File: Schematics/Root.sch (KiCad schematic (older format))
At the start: 2 parts

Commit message: Updated schematics
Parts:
- removed ANT1: ANT, Pin_Headers:Pin_Header_Straight_1x02, symbol INDUCTOR
- removed C1: C, symbol C
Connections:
- net labels added: SCL, SDA, VPP, Vusb, ~OE[0..12]
- net labels removed: GND
- wire segments 9 -> 7
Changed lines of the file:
@@
 LIBS:pca9685
 LIBS:avr_jtag_header
+LIBS:linear-technology
 LIBS:Root-cache
 EELAYER 25 0
@@
 $Descr A4 11693 8268
 encoding utf-8
-Sheet 1 17
+Sheet 1 16
 Title "RGB Clock"
 Date "Wed 07 Jan 2015"
@@
 $EndDescr
 $Sheet
-S 3850 2200 800  450
-U 54AA18DD
-F0 "Amp and Filter" 60
-F1 "BPF.sch" 60
-F2 "RF_in" I L 3850 2450 60
-F3 "RF_out" I R 4650 2450 60
-$EndSheet
-$Comp
-L INDUCTOR ANT1
-U 1 1 54AA1EFE
-P 3100 2800
-F 0 "ANT1" V 3050 2800 40  0000 C CNN
-F 1 "ANT" V 3200 2800 40  0000 C CNN
-F 2 "Pin_Headers:Pin_Header_Straight_1x02" H 3100 2800 60  0001 C CNN
-F 3 "" H 3100 2800 60  0000 C CNN
-	1    3100 2800
-	1    0    0    -1
-$EndComp
-$Comp
-L C C1
-U 1 1 54AA1FB2
-P 3400 2800
-F 0 "C1" H 3400 2900 40  0000 L CNN
-F 1 "C" H 3406 2715 40  0000 L CNN
-F 2 "" H 3438 2650 30  0001 C CNN
-F 3 "" H 3400 2800 60  0000 C CNN
-	1    3400 2800
-	1    0    0    -1
-$EndComp
-$Comp
-L GND #PWR01
-U 1 1 54AA202B
-P 3250 3200
-F 0 "#PWR01" H 3250 2950 60  0001 C CNN
-F 1 "GND" H 3250 3050 60  0000 C CNN
-F 2 "" H 3250 3200 60  0000 C CNN
-F 3 "" H 3250 3200 60  0000 C CNN
-	1    3250 3200
-	1    0    0    -1
-$EndComp
-Wire Wire Line
-	3250 3200 3250 3100
-Wire Wire Line
-	3100 3100 3400 3100
-Wire Wire Line
-	3400 3100 3400 3000
-Connection ~ 3250 3100
-Wire Wire Line
-	3100 2500 3100 2450
-Wire Wire Line
-	3100 2450 3850 2450
-Wire Wire Line
-	3400 2600 3400 2450
-Connection ~ 3400 2450
-$Sheet
 S 5300 2250 1150 600
 U 54B117F3
@@
 F2 "SDA" B R 6450 2600 60
 F3 "SCL" O R 6450 2750 60
-F4 "RF_In" I L 5300 2450 60
-F5 "~OE[1..12]" O R 6450 2450 60
+F4 "~OE[1..12]" O R 6450 2450 60
+F5 "Vusb" O L 5300 2700 60
+F6 "SNS[0..6]" I L 5300 2350 60
+F7 "SNSK[0..6]" I L 5300 2500 60
 $EndSheet
 $Sheet
@@
 $EndSheet
 $Sheet
-S 1900 4250 1500 1500
+S 5300 3400 1100 450
 U 54B1185F
 F0 "Power Supply" 60
 F1 "PowerSupply.sch" 60
+F2 "Vin" I L 5300 3600 60
+F3 "Vsupply" O R 6400 3600 60
 $EndSheet
 Wire Bus Line
@@
 Wire Wire Line
 	6450 2600 8000 2600
+$Comp
+L VPP #PWR02
+U 1 1 54BAF809
+P 6550 3550
+F 0 "#PWR02" H 6550 3400 60  0001 C CNN
+F 1 "VPP" H 6550 3700 60  0000 C CNN
+F 2 "" H 6550 3550 60  0000 C CNN
+F 3 "" H 6550 3550 60  0000 C CNN
+	1    6550 3550
+	1    0    0    -1
+$EndComp
 Wire Wire Line
-	4650 2450 5300 2450
+	5300 3600 5150 3600
+Wire Wire Line
+	5150 3600 5150 2700
+Wire Wire Line
+	5150 2700 5300 2700
+Wire Wire Line
+	6400 3600 6550 3600
+Wire Wire Line
+	6550 3600 6550 3550
+Text Label 7050 2450 0    60   ~ 0
+~OE[0..12]
+Text Label 7050 2600 0    60   ~ 0
+SDA
+Text Label 7050 2750 0    60   ~ 0
+SCL
+Text Label 5150 3200 0    60   ~ 0
+Vusb
 $EndSCHEMATC

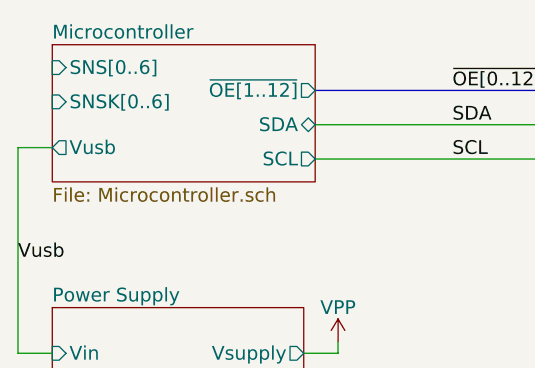
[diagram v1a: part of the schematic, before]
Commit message: Removed RF. Placed all LED drivers and passives and begun routing
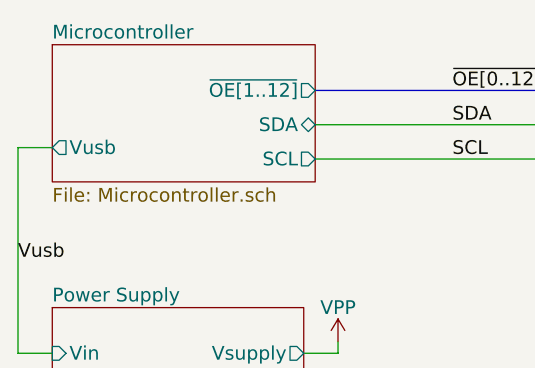
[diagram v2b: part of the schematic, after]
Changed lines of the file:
@@
 F4 "~OE[1..12]" O R 6450 2450 60
 F5 "Vusb" O L 5300 2700 60
-F6 "SNS[0..6]" I L 5300 2350 60
-F7 "SNSK[0..6]" I L 5300 2500 60
 $EndSheet
 $Sheet
@@
 	6450 2600 8000 2600
 $Comp
-L VPP #PWR02
+L VPP #PWR01
 U 1 1 54BAF809
 P 6550 3550
-F 0 "#PWR02" H 6550 3400 60  0001 C CNN
+F 0 "#PWR01" H 6550 3400 60  0001 C CNN
 F 1 "VPP" H 6550 3700 60  0000 C CNN
 F 2 "" H 6550 3550 60  0000 C CNN

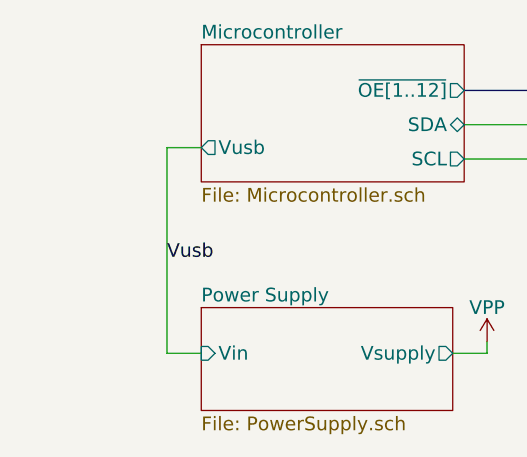
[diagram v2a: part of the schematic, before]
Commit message: Added power in connector in schematics. #3
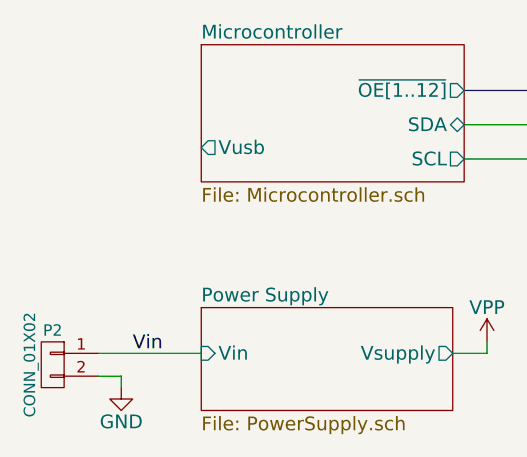
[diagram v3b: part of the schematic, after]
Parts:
- added P2: CONN_01X02, symbol CONN_01X02
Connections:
- new net GND: P2.2 (P2)
- new net Vin: P2.1 (P1)
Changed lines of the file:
@@
 	6450 2600 8000 2600
 $Comp
-L VPP #PWR01
+L VPP #PWR2
 U 1 1 54BAF809
 P 6550 3550
-F 0 "#PWR01" H 6550 3400 60  0001 C CNN
+F 0 "#PWR2" H 6550 3400 60  0001 C CNN
 F 1 "VPP" H 6550 3700 60  0000 C CNN
 F 2 "" H 6550 3550 60  0000 C CNN
@@
 $EndComp
 Wire Wire Line
-	5300 3600 5150 3600
-Wire Wire Line
-	5150 3600 5150 2700
-Wire Wire Line
-	5150 2700 5300 2700
+	4850 3600 5300 3600
 Wire Wire Line
 	6400 3600 6550 3600
@@
 Text Label 7050 2750 0    60   ~ 0
 SCL
-Text Label 5150 3200 0    60   ~ 0
-Vusb
+$Comp
+L CONN_01X02 P2
+U 1 1 54C94425
+P 4650 3650
+F 0 "P2" H 4650 3800 50  0000 C CNN
+F 1 "CONN_01X02" V 4750 3650 50  0000 C CNN
+F 2 "" H 4650 3650 60  0000 C CNN
+F 3 "" H 4650 3650 60  0000 C CNN
+	1    4650 3650
+	-1   0    0    -1
+$EndComp
+$Comp
+L GND #PWR1
+U 1 1 54C94A98
+P 4950 3750
+F 0 "#PWR1" H 4950 3500 60  0001 C CNN
+F 1 "GND" H 4950 3600 60  0000 C CNN
+F 2 "" H 4950 3750 60  0000 C CNN
+F 3 "" H 4950 3750 60  0000 C CNN
+	1    4950 3750
+	1    0    0    -1
+$EndComp
+Wire Wire Line
+	4850 3700 4950 3700
+Wire Wire Line
+	4950 3700 4950 3750
+Text Label 5000 3600 0    60   ~ 0
+Vin
 $EndSCHEMATC

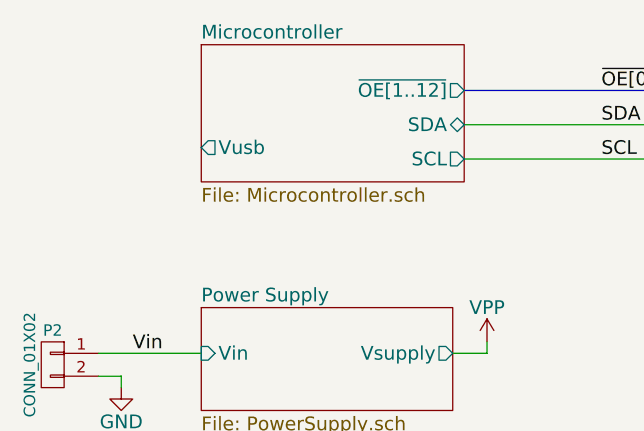
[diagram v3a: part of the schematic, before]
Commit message: Added some switches for interface #7
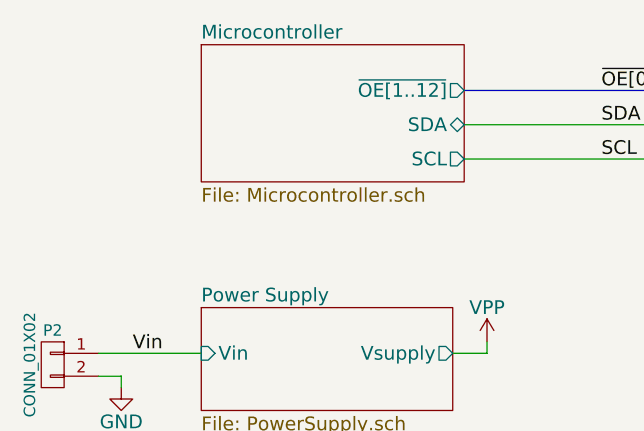
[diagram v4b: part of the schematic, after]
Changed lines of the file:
@@
 F3 "SCL" O R 6450 2750 60
 F4 "~OE[1..12]" O R 6450 2450 60
-F5 "Vusb" O L 5300 2700 60
 $EndSheet
 $Sheet

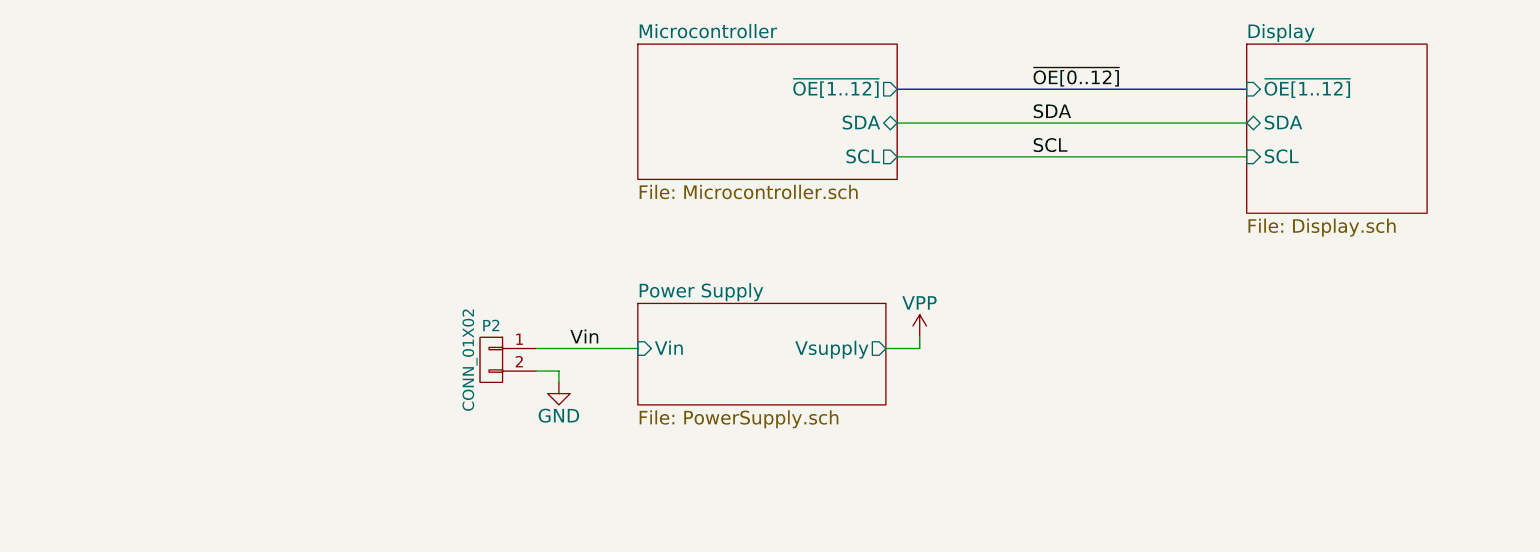
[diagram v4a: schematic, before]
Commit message: Changed lots
Finalised the Inductor. Closes #5
Changed USB Connector. Closes #4
Added four switches for a simple interface. Closes #7
Added a power jack. Closes #3
Found RTC Oscillator. Closes #1.
Added part numbers to all major components. Closes #2
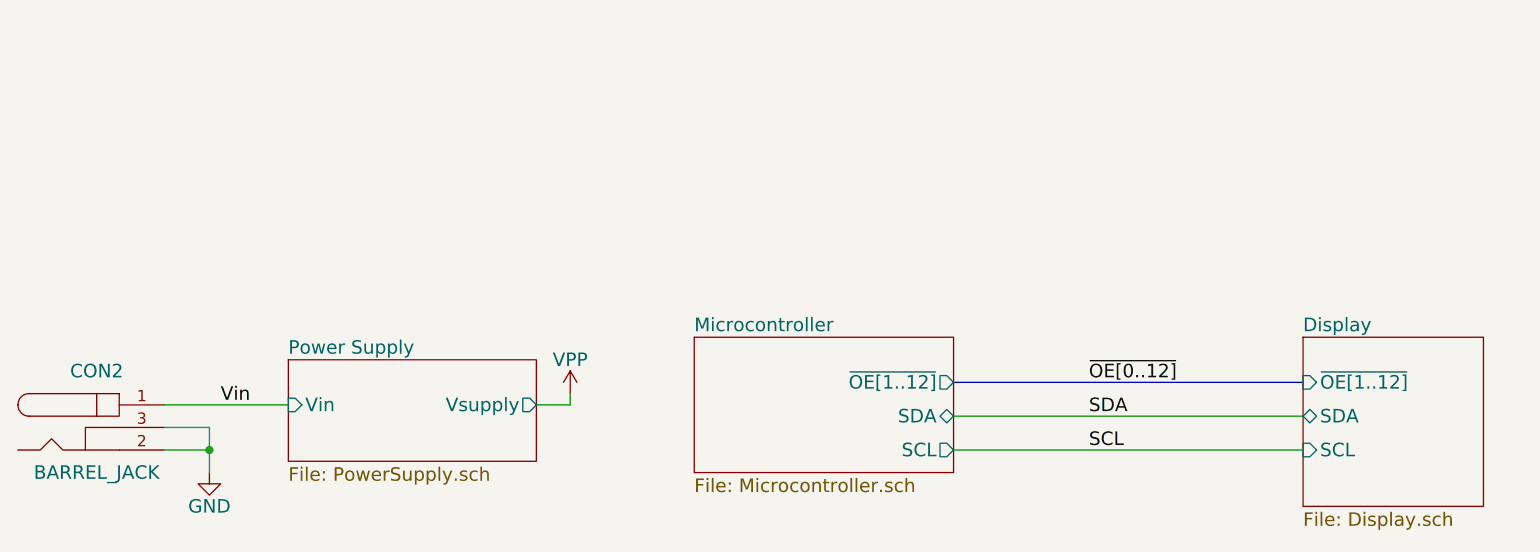
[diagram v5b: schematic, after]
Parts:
- removed P2: CONN_01X02, symbol CONN_01X02
- added CON2: BARREL_JACK, Connect:JACK_ALIM, symbol BARREL_JACK
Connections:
- net GND: now also CON2.2, CON2.3
- net Vin: now also CON2.1
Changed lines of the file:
@@
 $EndDescr
 $Sheet
-S 5300 2250 1150 600
+S 5550 3550 1150 600
 U 54B117F3
 F0 "Microcontroller" 60
 F1 "Microcontroller.sch" 60
-F2 "SDA" B R 6450 2600 60
-F3 "SCL" O R 6450 2750 60
-F4 "~OE[1..12]" O R 6450 2450 60
+F2 "SDA" B R 6700 3900 60
+F3 "SCL" O R 6700 4050 60
+F4 "~OE[1..12]" O R 6700 3750 60
 $EndSheet
 $Sheet
-S 8000 2250 800  750
+S 8250 3550 800  750
 U 54B11834
 F0 "Display" 60
 F1 "Display.sch" 60
-F2 "SDA" B L 8000 2600 60
-F3 "SCL" I L 8000 2750 60
-F4 "~OE[1..12]" I L 8000 2450 60
+F2 "SDA" B L 8250 3900 60
+F3 "SCL" I L 8250 4050 60
+F4 "~OE[1..12]" I L 8250 3750 60
 $EndSheet
 $Sheet
-S 5300 3400 1100 450
+S 3750 3650 1100 450
 U 54B1185F
 F0 "Power Supply" 60
 F1 "PowerSupply.sch" 60
-F2 "Vin" I L 5300 3600 60
-F3 "Vsupply" O R 6400 3600 60
+F2 "Vin" I L 3750 3850 60
+F3 "Vsupply" O R 4850 3850 60
 $EndSheet
 Wire Bus Line
-	6450 2450 8000 2450
+	6700 3750 8250 3750
 Wire Wire Line
-	8000 2750 6450 2750
+	8250 4050 6700 4050
 Wire Wire Line
-	6450 2600 8000 2600
+	6700 3900 8250 3900
 $Comp
-L VPP #PWR2
+L VPP #PWR01
 U 1 1 54BAF809
-P 6550 3550
-F 0 "#PWR2" H 6550 3400 60  0001 C CNN
-F 1 "VPP" H 6550 3700 60  0000 C CNN
-F 2 "" H 6550 3550 60  0000 C CNN
-F 3 "" H 6550 3550 60  0000 C CNN
-	1    6550 3550
+P 5000 3800
+F 0 "#PWR01" H 5000 3650 60  0001 C CNN
+F 1 "VPP" H 5000 3950 60  0000 C CNN
+F 2 "" H 5000 3800 60  0000 C CNN
+F 3 "" H 5000 3800 60  0000 C CNN
+	1    5000 3800
 	1    0    0    -1
 $EndComp
 Wire Wire Line
-	4850 3600 5300 3600
+	3200 3850 3750 3850
 Wire Wire Line
-	6400 3600 6550 3600
+	4850 3850 5000 3850
 Wire Wire Line
-	6550 3600 6550 3550
-Text Label 7050 2450 0    60   ~ 0
+	5000 3850 5000 3800
+Text Label 7300 3750 0    60   ~ 0
 ~OE[0..12]
-Text Label 7050 2600 0    60   ~ 0
+Text Label 7300 3900 0    60   ~ 0
 SDA
-Text Label 7050 2750 0    60   ~ 0
+Text Label 7300 4050 0    60   ~ 0
 SCL
 $Comp
-L CONN_01X02 P2
-U 1 1 54C94425
-P 4650 3650
-F 0 "P2" H 4650 3800 50  0000 C CNN
-F 1 "CONN_01X02" V 4750 3650 50  0000 C CNN
-F 2 "" H 4650 3650 60  0000 C CNN
-F 3 "" H 4650 3650 60  0000 C CNN
-	1    4650 3650
-	-1   0    0    -1
-$EndComp
-$Comp
-L GND #PWR1
+L GND #PWR02
 U 1 1 54C94A98
-P 4950 3750
-F 0 "#PWR1" H 4950 3500 60  0001 C CNN
-F 1 "GND" H 4950 3600 60  0000 C CNN
-F 2 "" H 4950 3750 60  0000 C CNN
-F 3 "" H 4950 3750 60  0000 C CNN
-	1    4950 3750
+P 3400 4150
+F 0 "#PWR02" H 3400 3900 60  0001 C CNN
+F 1 "GND" H 3400 4000 60  0000 C CNN
+F 2 "" H 3400 4150 60  0000 C CNN
+F 3 "" H 3400 4150 60  0000 C CNN
+	1    3400 4150
 	1    0    0    -1
 $EndComp
 Wire Wire Line
-	4850 3700 4950 3700
+	3200 3950 3400 3950
 Wire Wire Line
-	4950 3700 4950 3750
-Text Label 5000 3600 0    60   ~ 0
+	3400 3950 3400 4150
+Text Label 3450 3850 0    60   ~ 0
 Vin
+$Comp
+L BARREL_JACK CON2
+U 1 1 54C9C7E5
+P 2900 3950
+F 0 "CON2" H 2900 4200 60  0000 C CNN
+F 1 "BARREL_JACK" H 2900 3750 60  0000 C CNN
+F 2 "Connect:JACK_ALIM" H 2900 3950 60  0001 C CNN
+F 3 "http://dlnmh9ip6v2uc.cloudfront.net/datasheets/Prototyping/18742.pdf" H 2900 3950 60  0001 C CNN
+F 4 "PRT-10811" H 2900 3950 60  0001 C CNN "Part"
+F 5 "SparkFun" H 2900 3950 60  0001 C CNN "Supplier"
+	1    2900 3950
+	1    0    0    -1
+$EndComp
+Wire Wire Line
+	3400 4050 3200 4050
+Connection ~ 3400 4050
 $EndSCHEMATC

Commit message: Started Redesign.
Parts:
- added P1, P10, P11, P12, P2, P3, P4, P5, P6, P7, P8, P9: CONN_01X06, symbol CONN_01X06
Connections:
- net GND: now also P1.4 (P4), P1.6 (P6), P10.4 (P4), P10.6 (P6), P11.4 (P4), P11.6 (P6), P12.4 (P4), P12.6 (P6), P2.4 (P4), P2.6 (P6), P3.4 (P4), P3.6 (P6), P4.4 (P4), P4.6 (P6), P5.4 (P4), P5.6 (P6), P6.4 (P4), P6.6 (P6), P7.4 (P4), P7.6 (P6), P8.4 (P4), P8.6 (P6), P9.4 (P4), P9.6 (P6)
- net SCL: now also P1.3 (P3), P10.3 (P3), P11.3 (P3), P12.3 (P3), P2.3 (P3), P3.3 (P3), P4.3 (P3), P5.3 (P3), P6.3 (P3), P7.3 (P3), P8.3 (P3), P9.3 (P3)
- net SDA: now also P1.2 (P2), P10.2 (P2), P11.2 (P2), P12.2 (P2), P2.2 (P2), P3.2 (P2), P4.2 (P2), P5.2 (P2), P6.2 (P2), P7.2 (P2), P8.2 (P2), P9.2 (P2)
- net VPP: now also P1.1 (P1), P10.1 (P1), P11.1 (P1), P12.1 (P1), P2.1 (P1), P3.1 (P1), P4.1 (P1), P5.1 (P1), P6.1 (P1), P7.1 (P1), P8.1 (P1), P9.1 (P1)
- new net ~OE1: P1.5 (P5)
- new net ~OE10: P10.5 (P5)
- new net ~OE11: P11.5 (P5)
- new net ~OE12: P12.5 (P5)
- new net ~OE2: P2.5 (P5)
- new net ~OE3: P3.5 (P5)
- new net ~OE4: P4.5 (P5)
- new net ~OE5: P5.5 (P5)
- new net ~OE6: P6.5 (P5)
- new net ~OE7: P7.5 (P5)
- new net ~OE8: P8.5 (P5)
- new net ~OE9: P9.5 (P5)
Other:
- moved on the sheet: CON2

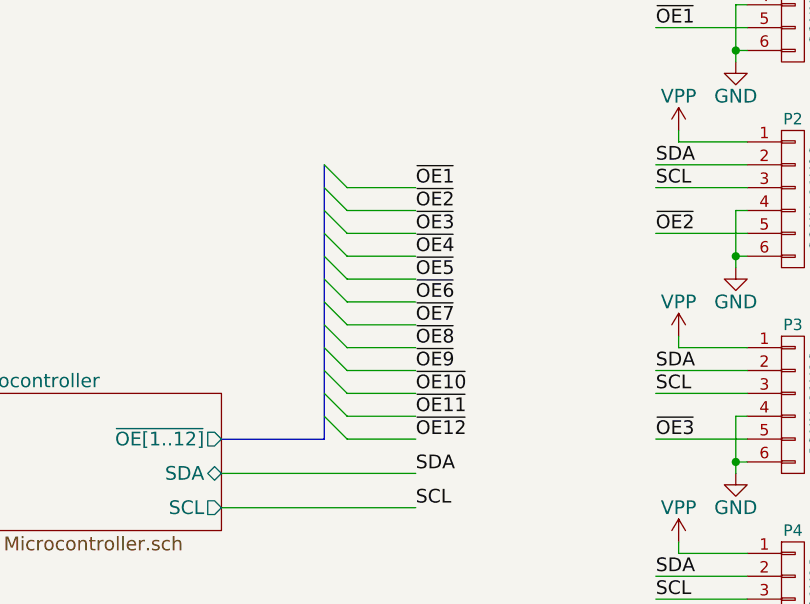
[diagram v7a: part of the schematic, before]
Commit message: Done some more layout.
Need to sort pin swaps for the OE lines and complete routing
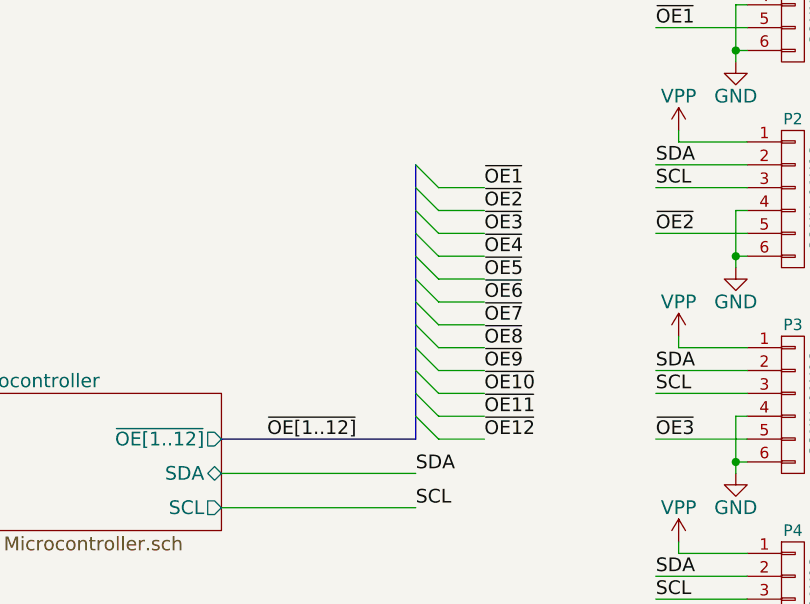
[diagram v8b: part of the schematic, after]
